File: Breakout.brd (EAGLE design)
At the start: 80 x 100 mm, 177 parts, among them IC1 LM337LZ, IC2 78L05SMD, U1 ADS131E08, U11 TC1014, U12 LTC6655, U2 TLV433, U3 TLV433, U4 TLV433, U5 TLV433, U6 TLV433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

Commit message: Op-amp Power Routed
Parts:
- added C83: 1µ, resistor:C0603
- moved C69 2.00 mm to (24.0, 32.5)
- moved U12 2.00 mm to (28.5, 32.5)
- moved X3 1.12 mm to (5.50, 33.5), turned to 90 degrees
- turned R1 to 90 degrees
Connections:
- new net PAS3: C37.1, JP9.2, R17.2, U4.5
- new net PAS4: C43.1, JP10.2, R21.2, U5.5
- new net PAS5: C49.1, JP15.2, R25.2, U6.5
- new net PAS6: C55.1, JP16.2, R29.2, U7.5
- new net PAS7: C61.1, JP19.2, R33.2, U8.5
- new net PAS8: C67.1, JP20.2, R37.2, U9.5
- net PAS1: no longer C37.1, C49.1, C61.1, JP15.2, JP19.2, JP9.2, R17.2, R25.2, R33.2, U4.5, U6.5, U8.5
- net PAS2: no longer C43.1, C55.1, C67.1, JP10.2, JP16.2, JP20.2, R21.2, R29.2, R37.2, U5.5, U7.5, U9.5
- net VCC: now also C83.1
- net VSS: now also C83.2
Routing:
- net VSS: track 171.7 -> 346.9 mm, vias 4 -> 14
- net VCC: track 218.9 -> 352.5 mm, vias 2 -> 17
- net PAS2: track 175.1 -> 43.8 mm
- net PAS1: track 123.2 -> 30.8 mm
- net PAS6: track 0.00 -> 42.9 mm
- net PAS8: track 0.00 -> 42.9 mm
- net PAS4: track 0.00 -> 42.9 mm
- net PAS3: track 0.00 -> 30.2 mm
- net PAS7: track 0.00 -> 30.2 mm
- net PAS5: track 0.00 -> 30.2 mm
- net VREF: track 34.1 -> 30.1 mm
- net AIN2: track 47.9 -> 45.3 mm
- net -AIN2: track 49.7 -> 47.3 mm
- net -AIN7: track 26.0 -> 24.7 mm
- net RST: track 38.8 -> 37.6 mm
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
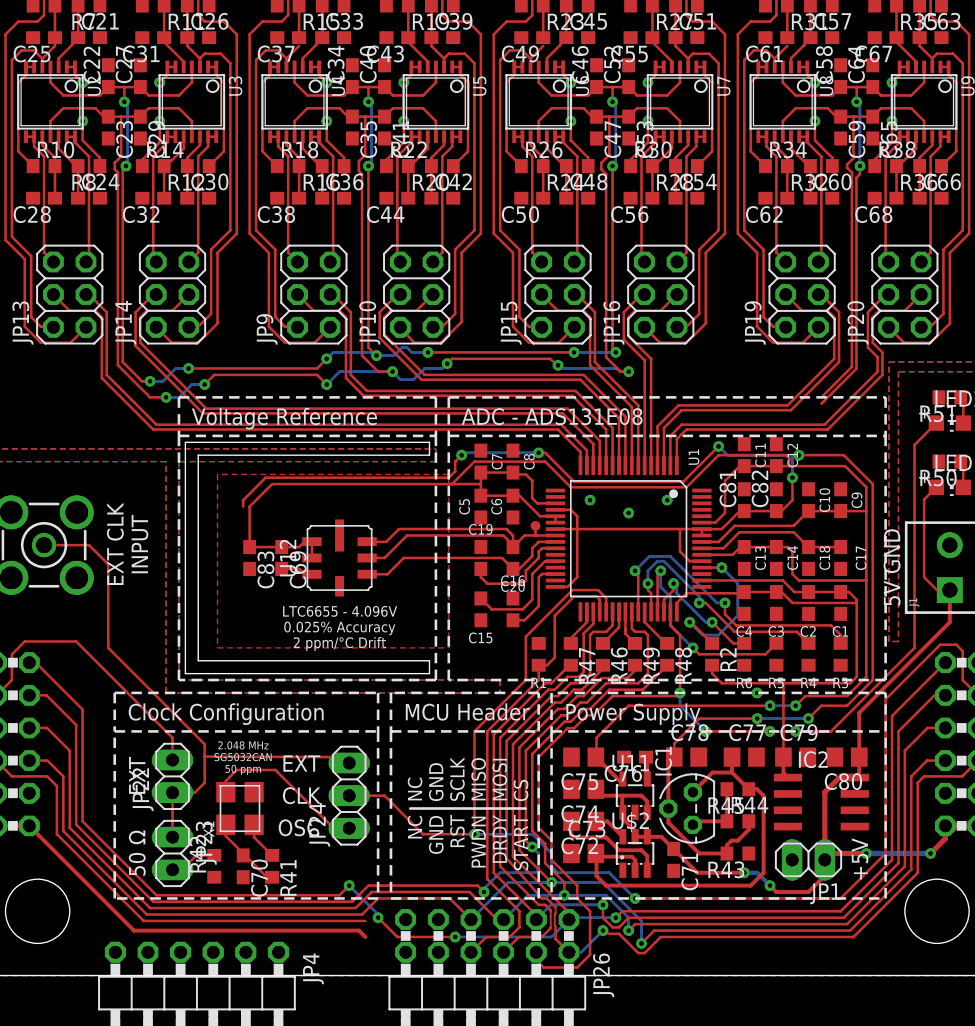
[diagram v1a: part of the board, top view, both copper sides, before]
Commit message: Op-amp Power Supply Routing Finished
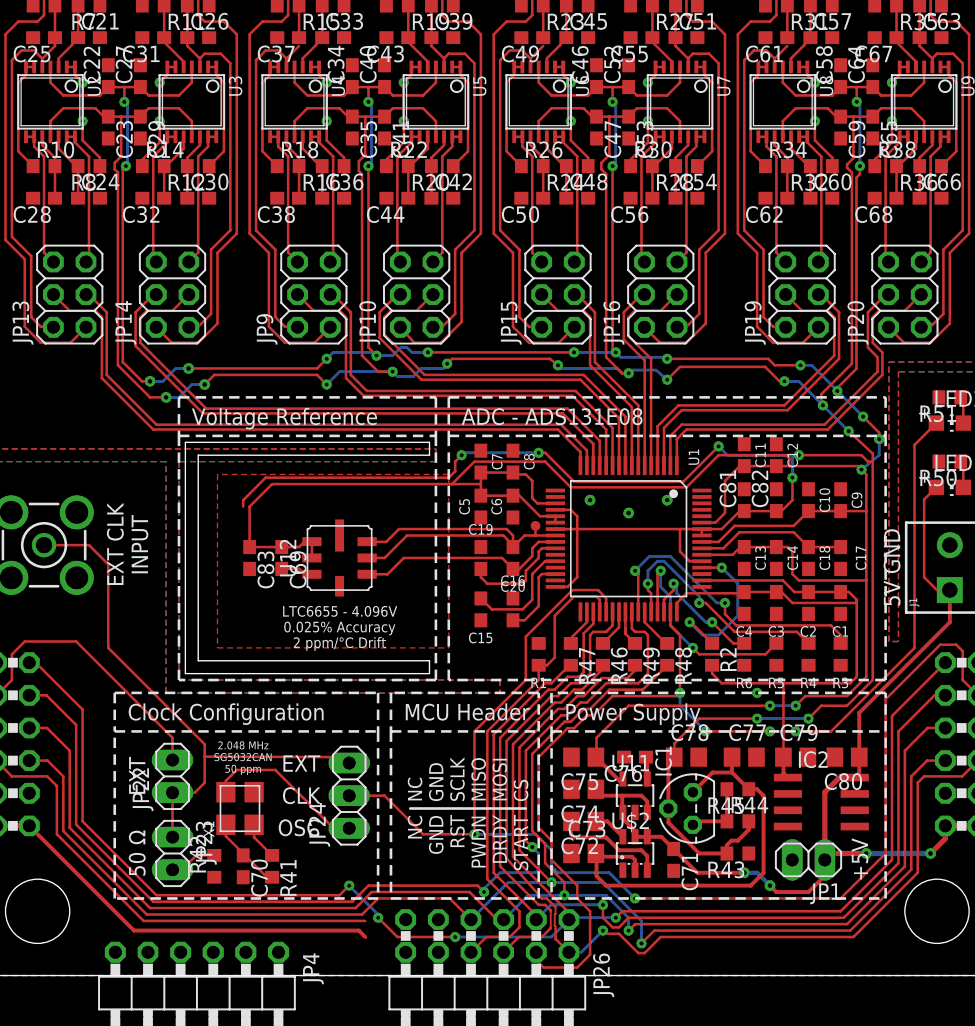
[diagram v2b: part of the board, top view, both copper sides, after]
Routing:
- net VCC: track 352.5 -> 378.2 mm, vias 17 -> 23
- net VSS: track 346.9 -> 371.8 mm, vias 14 -> 18

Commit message: Clean PSU
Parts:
- added C84, C86: 100µ, passives-custom:UWT1C-6.3X5.4
- added C85, C87: 1µ, resistor:C0805
- added L1, L2: 180µ, passives-custom:NPIM104P
- added Q1, Q2: 2N3904, transistor-small-signal:TO92D
- added Q3, Q4: 2N3906, transistor-small-signal:TO92D
- added R39, R40: 330, resistor:R0603
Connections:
- new net N$6436: C73.2, U$2.2
- new net N$6440: L1.P$2, R39.2
- new net N$6441: C84.+, L1.P$1, Q1.B
- new net N$6442: Q1.E, Q2.B
- new net N$6443: C86.+, L2.P$1, Q3.B
- new net N$6446: Q1.C, Q2.C, R39.1
- new net N$6447: C85.1, Q2.E
- new net N$6448: L2.P$2, R40.2
- new net N$6449: Q3.E, Q4.B
- new net N$6450: Q3.C, Q4.C, R40.1
- new net N$6451: C87.1, Q4.E
- net -5V: no longer C73.2, U$2.2
- net GND: now also C84.-, C85.2, C86.-, C87.2
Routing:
- net -5V: track 33.5 -> 32.5 mm
